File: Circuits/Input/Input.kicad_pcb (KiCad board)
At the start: 2 copper layers, 28.9 x 68.9 mm, 9 parts, among them J1 sensor, P1 WRITER-VCC, SW1 MKA-10110, U1 TWELITE_SMD

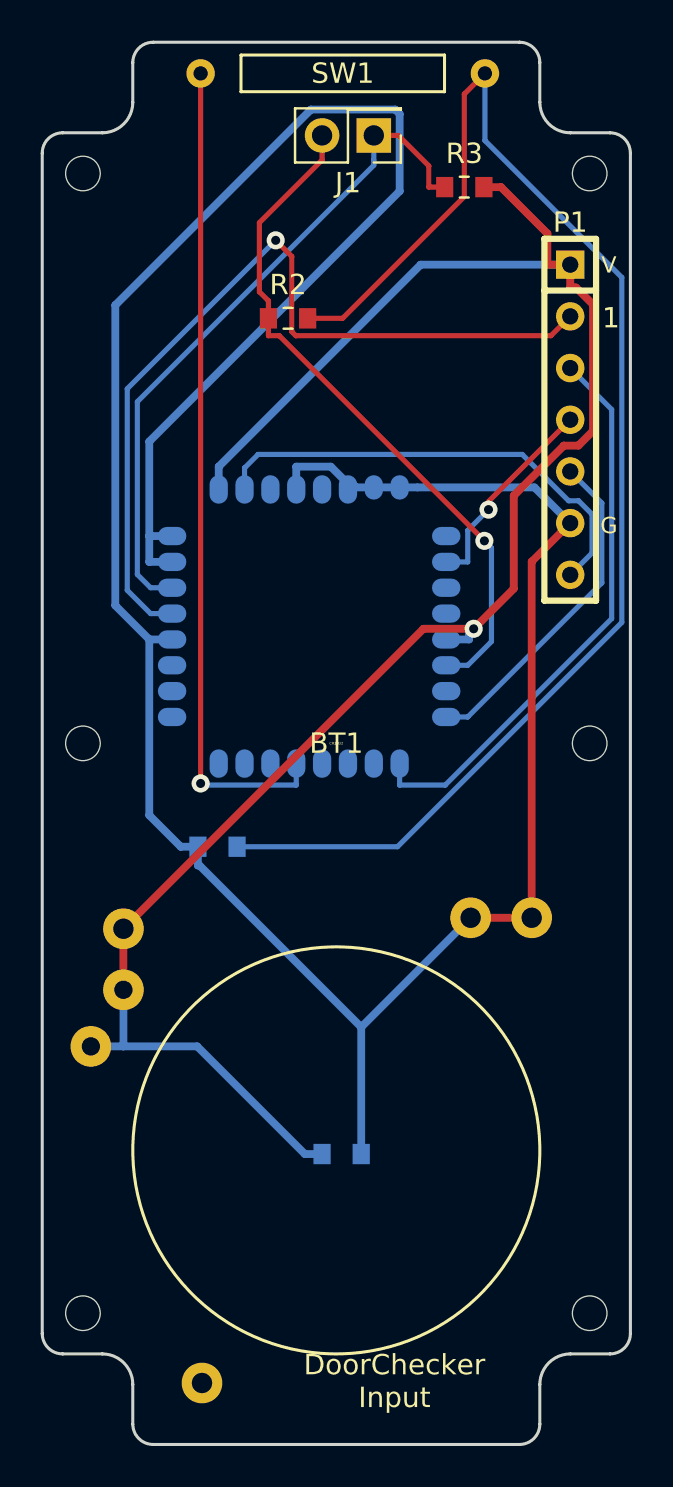
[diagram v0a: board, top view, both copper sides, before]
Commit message: ADC2をGNDに配線
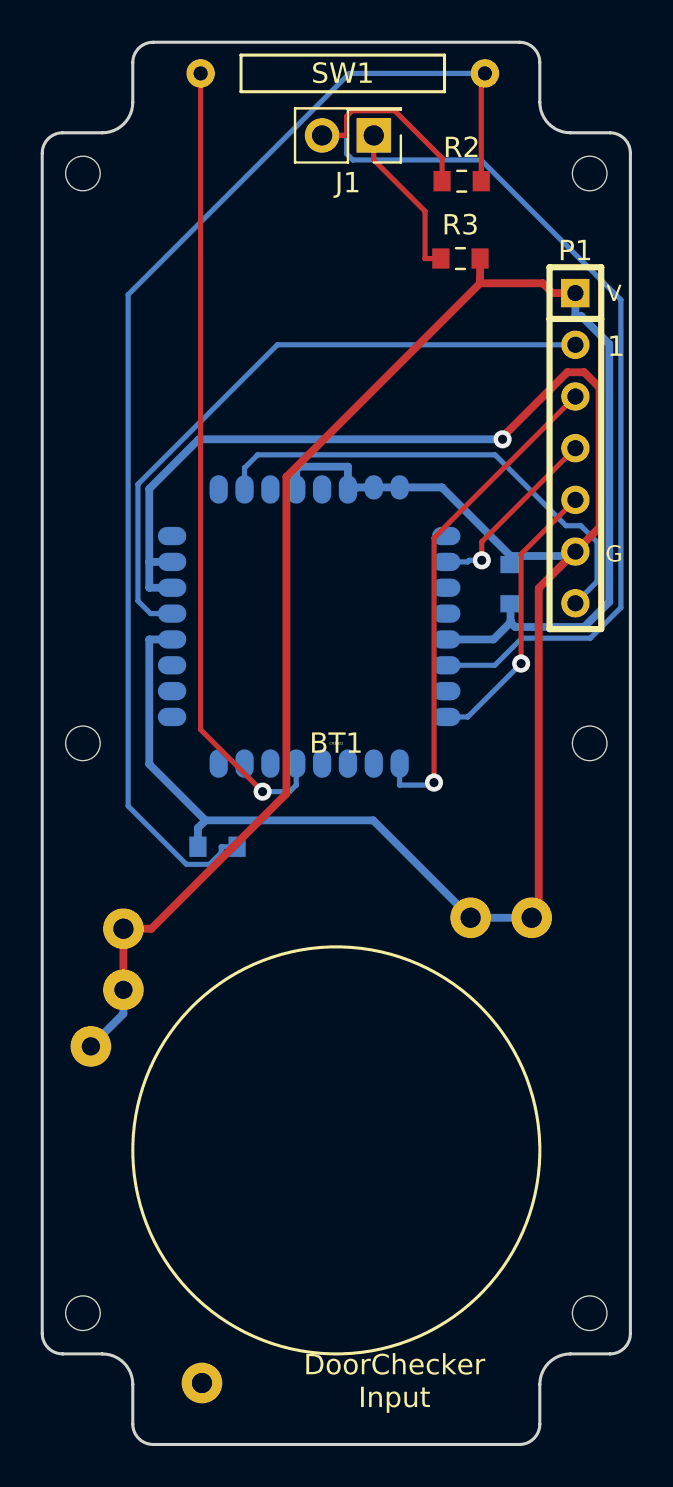
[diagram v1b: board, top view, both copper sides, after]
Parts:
- moved C1 29.2 mm to (37.2, 41.1), turned to 90 degrees
- moved R2 10.9 mm to (34.8, 21.3)
- moved R3 3.52 mm to (34.7, 25.1)
- moved P1 1.42 mm to (40.4, 34.4)
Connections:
- U1 pad 22: Net-(J1-Pad1) -> GND
- U1 pad 24: GND -> Net-(U1-Pad24)
- U1 pad 25: /Vcc -> Net-(U1-Pad25)
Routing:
- net GND: track 142.6 -> 107.8 mm, vias 0 -> 1
- net Net-(J1-Pad1): track 33.5 -> 7.87 mm
- net Net-(J1-Pad2): track 33.9 -> 52.5 mm, vias 1 -> 0
- net /Vcc: track 95.0 -> 78.2 mm, vias 1 -> 0
- net Net-(R1-Pad1): track 69.9 -> 59.6 mm
- net /RST: track 41.9 -> 32.0 mm, vias 1 -> 0
- net /RXD: track 28.0 -> 24.6 mm, vias 0 -> 1
- net /TXD: track 16.5 -> 13.9 mm, vias 0 -> 1
- net /DI1: track 40.7 -> 39.4 mm
- net /PRG: track 10.1 -> 9.19 mm
- net /CFG: track 23.0 -> 23.9 mm
